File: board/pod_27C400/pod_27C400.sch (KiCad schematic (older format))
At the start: 13 parts, among them J1 EXT_D, J2 EXT_ADDR, J3 VCC_Probe, J4 GND_Probe, J5 ROM Lines, U1 74HCT02

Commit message: Added pod for 27C400, modified other pods
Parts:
- removed J5: ROM Lines, Connector_PinHeader_2.54mm:PinHeader_2x14_P2.54mm_Vertical, symbol Connector_Generic:Conn_02x14_Odd_Even
- added J5: ROM Lines, Connector_PinHeader_2.54mm:PinHeader_2x20_P2.54mm_Vertical, symbol Connector_Generic:Conn_02x20_Odd_Even
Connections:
- wire segments 203 -> 216
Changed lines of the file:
@@
 Wire Wire Line
 	7050 2100 7200 2100
-$Comp
-L Connector_Generic:Conn_02x14_Odd_Even J5
-U 1 1 5FE5E217
-P 6500 3700
-F 0 "J5" H 6550 4517 50  0000 C CNN
-F 1 "ROM Lines" H 6550 4426 50  0000 C CNN
-F 2 "Connector_PinHeader_2.54mm:PinHeader_2x14_P2.54mm_Vertical" H 6500 3700 50  0001 C CNN
-F 3 "~" H 6500 3700 50  0001 C CNN
-	1    6500 3700
-	1    0    0    -1
-$EndComp
-Wire Wire Line
-	6800 3100 7200 3100
-Text Label 7200 3100 2    50   ~ 0
+Wire Wire Line
+	6950 5000 7350 5000
+Text Label 7350 5000 2    50   ~ 0
 EXT_VCC
-Wire Wire Line
-	6800 3200 7200 3200
-Wire Wire Line
-	6800 3300 7200 3300
-Wire Wire Line
-	6800 3400 7200 3400
-Wire Wire Line
-	6800 3500 7200 3500
-Wire Wire Line
-	6800 3600 7200 3600
-Wire Wire Line
-	6800 3700 7200 3700
-Wire Wire Line
-	6800 3800 7200 3800
-Wire Wire Line
-	6800 3900 7200 3900
-Wire Wire Line
-	6800 4000 7200 4000
-Wire Wire Line
-	6800 4100 7200 4100
-Wire Wire Line
-	6800 4200 7200 4200
-Wire Wire Line
-	6800 4300 7200 4300
-Wire Wire Line
-	6800 4400 7200 4400
-Wire Wire Line
-	6300 3100 5800 3100
-Wire Wire Line
-	6300 3200 5800 3200
-Wire Wire Line
-	6300 3300 5800 3300
-Wire Wire Line
-	6300 3400 5800 3400
-Wire Wire Line
-	6300 3500 5800 3500
-Wire Wire Line
-	6300 3600 5800 3600
-Wire Wire Line
-	6300 3700 5800 3700
-Wire Wire Line
-	6300 3800 5800 3800
-Wire Wire Line
-	6300 3900 5800 3900
-Wire Wire Line
-	6300 4000 5800 4000
-Wire Wire Line
-	6300 4100 5800 4100
-Wire Wire Line
-	6300 4200 5800 4200
-Wire Wire Line
-	6300 4300 5800 4300
-Wire Wire Line
-	6300 4400 5800 4400
 $Comp
 L power:GND #PWR0113
 U 1 1 5FFADC5E
-P 5800 4500
-F 0 "#PWR0113" H 5800 4250 50  0001 C CNN
-F 1 "GND" H 5805 4327 50  0000 C CNN
-F 2 "" H 5800 4500 50  0001 C CNN
-F 3 "" H 5800 4500 50  0001 C CNN
-	1    5800 4500
-	1    0    0    -1
-$EndComp
-Wire Wire Line
-	5800 4400 5800 4500
-Text Label 5800 3100 0    50   ~ 0
-A15
-Text Label 5800 3200 0    50   ~ 0
-A12
-Text Label 5800 3300 0    50   ~ 0
-A7
-Text Label 5800 3400 0    50   ~ 0
-A6
-Text Label 5800 3500 0    50   ~ 0
-A5
-Text Label 5800 3600 0    50   ~ 0
-A4
-Text Label 5800 3700 0    50   ~ 0
-A3
-Text Label 5800 3800 0    50   ~ 0
-A2
-Text Label 5800 3900 0    50   ~ 0
-A1
-Text Label 5800 4000 0    50   ~ 0
-A0
-Text Label 5800 4100 0    50   ~ 0
-D0
-Text Label 5800 4200 0    50   ~ 0
-D1
-Text Label 5800 4300 0    50   ~ 0
-D2
-Text Label 7200 4400 2    50   ~ 0
-D3
-Text Label 7200 4300 2    50   ~ 0
-D4
-Text Label 7200 4200 2    50   ~ 0
-D5
-Text Label 7200 4100 2    50   ~ 0
-D6
-Text Label 7200 4000 2    50   ~ 0
-D7
-Text Label 7200 3900 2    50   ~ 0
-~DIR_CE
-Text Label 7200 3800 2    50   ~ 0
-A10
-Text Label 7200 3700 2    50   ~ 0
-~OE
-Text Label 7200 3600 2    50   ~ 0
-A11
-Text Label 7200 3500 2    50   ~ 0
-A9
-Text Label 7200 3400 2    50   ~ 0
-A8
-Text Label 7200 3300 2    50   ~ 0
-A13
-Text Label 7200 3200 2    50   ~ 0
-A14
+P 7550 4200
+F 0 "#PWR0113" H 7550 3950 50  0001 C CNN
+F 1 "GND" H 7555 4027 50  0000 C CNN
+F 2 "" H 7550 4200 50  0001 C CNN
+F 3 "" H 7550 4200 50  0001 C CNN
+	1    7550 4200
+	1    0    0    -1
+$EndComp
 $Comp
 L Device:LED_Small D1
@@
 Wire Wire Line
 	1950 3000 2250 3000
+$Comp
+L Connector_Generic:Conn_02x20_Odd_Even J5
+U 1 1 5FFBAEB6
+P 6650 4000
+F 0 "J5" H 6700 5117 50  0000 C CNN
+F 1 "ROM Lines" H 6700 5026 50  0000 C CNN
+F 2 "Connector_PinHeader_2.54mm:PinHeader_2x20_P2.54mm_Vertical" H 6650 4000 50  0001 C CNN
+F 3 "~" H 6650 4000 50  0001 C CNN
+	1    6650 4000
+	1    0    0    -1
+$EndComp
+Wire Wire Line
+	7550 4100 7550 4200
+$Comp
+L power:GND #PWR?
+U 1 1 60054FB5
+P 5900 4200
+F 0 "#PWR?" H 5900 3950 50  0001 C CNN
+F 1 "GND" H 5905 4027 50  0000 C CNN
+F 2 "" H 5900 4200 50  0001 C CNN
+F 3 "" H 5900 4200 50  0001 C CNN
+	1    5900 4200
+	1    0    0    -1
+$EndComp
+Wire Wire Line
+	5900 4100 5900 4200
+Wire Wire Line
+	6950 4000 7450 4000
+Text Label 7450 4000 2    50   ~ 0
+A18
+Wire Wire Line
+	6950 3100 7450 3100
+Wire Wire Line
+	6950 3200 7450 3200
+Wire Wire Line
+	6950 3300 7450 3300
+Wire Wire Line
+	6950 3400 7450 3400
+Wire Wire Line
+	6950 3500 7450 3500
+Wire Wire Line
+	6950 3600 7450 3600
+Wire Wire Line
+	6950 3700 7450 3700
+Wire Wire Line
+	6950 3800 7450 3800
+Wire Wire Line
+	6950 3900 7450 3900
+Wire Wire Line
+	6950 4100 7550 4100
+Wire Wire Line
+	6950 4200 7450 4200
+Wire Wire Line
+	6950 4300 7450 4300
+Wire Wire Line
+	6950 4400 7450 4400
+Wire Wire Line
+	6950 4500 7450 4500
+Wire Wire Line
+	6950 4600 7450 4600
+Wire Wire Line
+	6950 4700 7450 4700
+Wire Wire Line
+	6950 4800 7450 4800
+Wire Wire Line
+	6950 4900 7450 4900
+Text Label 7450 3100 2    50   ~ 0
+A8
+Text Label 7450 3200 2    50   ~ 0
+A9
+Text Label 7450 3300 2    50   ~ 0
+A10
+Text Label 7450 3400 2    50   ~ 0
+A11
+Text Label 7450 3500 2    50   ~ 0
+A12
+Text Label 7450 3600 2    50   ~ 0
+A13
+Text Label 7450 3700 2    50   ~ 0
+A14
+Text Label 7450 3800 2    50   ~ 0
+A15
+Text Label 7450 3900 2    50   ~ 0
+A16
+Wire Wire Line
+	6450 3100 6000 3100
+Wire Wire Line
+	6450 3200 6000 3200
+Wire Wire Line
+	6450 3300 6000 3300
+Wire Wire Line
+	6450 3400 6000 3400
+Wire Wire Line
+	6450 3500 6000 3500
+Wire Wire Line
+	6450 3600 6000 3600
+Wire Wire Line
+	6450 3700 6000 3700
+Wire Wire Line
+	6450 3800 6000 3800
+Wire Wire Line
+	6450 3900 6000 3900
+Wire Wire Line
+	6450 4000 6000 4000
+Wire Wire Line
+	6450 4200 6000 4200
+Wire Wire Line
+	6450 4300 6000 4300
+Wire Wire Line
+	6450 4400 6000 4400
+Wire Wire Line
+	6450 4500 6000 4500
+Wire Wire Line
+	6450 4600 6000 4600
+Wire Wire Line
+	6450 4700 6000 4700
+Wire Wire Line
+	6450 4800 6000 4800
+Wire Wire Line
+	6450 4900 6000 4900
+Wire Wire Line
+	6450 5000 6000 5000
+Text Label 6000 3100 0    50   ~ 0
+A17
+Text Label 6000 3200 0    50   ~ 0
+A7
+Text Label 6000 3300 0    50   ~ 0
+A6
+Text Label 6000 3400 0    50   ~ 0
+A5
+Text Label 6000 3500 0    50   ~ 0
+A4
+Text Label 6000 3600 0    50   ~ 0
+A3
+Text Label 6000 3700 0    50   ~ 0
+A2
+Text Label 6000 3800 0    50   ~ 0
+A1
+Text Label 6000 3900 0    50   ~ 0
+A0
+Text Label 6000 4000 0    50   ~ 0
+~DIR_CE
+Wire Wire Line
+	5900 4100 6450 4100
+Text Label 6000 4200 0    50   ~ 0
+~OE
+Text Label 6000 4300 0    50   ~ 0
+D0
+Text Label 6000 4400 0    50   ~ 0
+D8
+Text Label 6000 4500 0    50   ~ 0
+D1
+Text Label 6000 4600 0    50   ~ 0
+D9
+Text Label 6000 4700 0    50   ~ 0
+D2
+Text Label 6000 4800 0    50   ~ 0
+D10
+Text Label 6000 4900 0    50   ~ 0
+D3
+Text Label 6000 5000 0    50   ~ 0
+D11
+Text Label 7450 4900 2    50   ~ 0
+D4
+Text Label 7450 4800 2    50   ~ 0
+D12
+Text Label 7450 4700 2    50   ~ 0
+D5
+Text Label 7450 4600 2    50   ~ 0
+D13
+Text Label 7450 4500 2    50   ~ 0
+D6
+Text Label 7450 4400 2    50   ~ 0
+D14
+Text Label 7450 4300 2    50   ~ 0
+D7
+Text Label 7450 4200 2    50   ~ 0
+D15
 $EndSCHEMATC

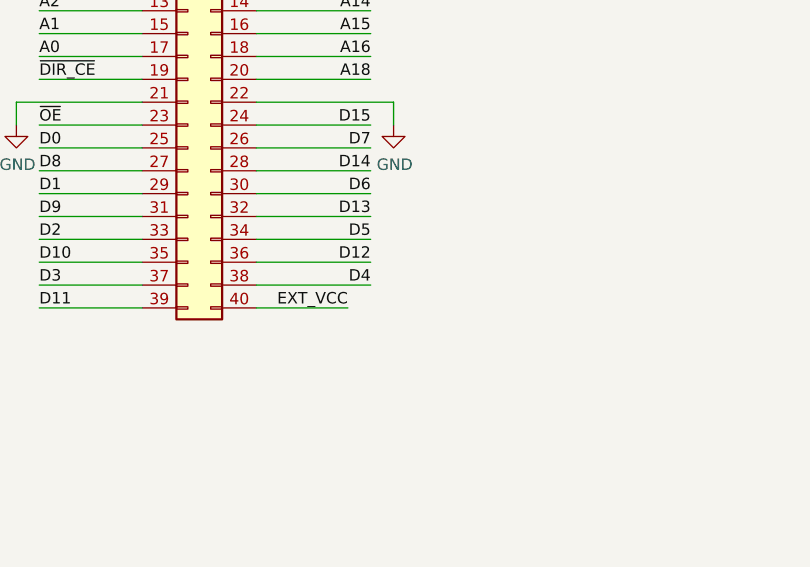
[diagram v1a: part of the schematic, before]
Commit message: Update all the pods to include the diode
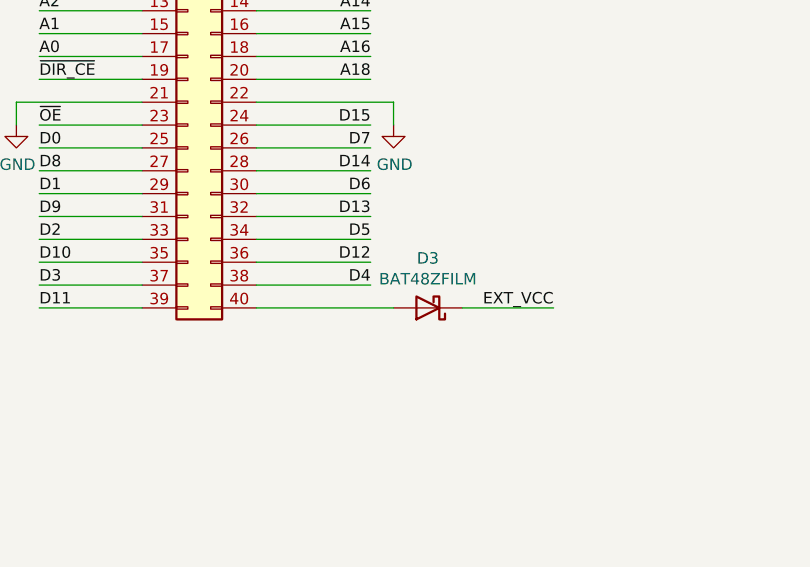
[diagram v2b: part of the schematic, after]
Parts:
- added D3: BAT48ZFILM, Diode_SMD:D_SOD-123, symbol Diode:BAT48ZFILM
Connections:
- net EXT_VCC: now also D3.1 (K); no longer J5.40 (Pin_40)
- new net: D3.2 (A), J5.40 (Pin_40)
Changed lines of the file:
@@
 	7050 2100 7200 2100
 Wire Wire Line
-	6950 5000 7350 5000
-Text Label 7350 5000 2    50   ~ 0
+	7850 5000 8250 5000
+Text Label 8250 5000 2    50   ~ 0
 EXT_VCC
 $Comp
@@
 	7550 4100 7550 4200
 $Comp
-L power:GND #PWR?
+L power:GND #PWR0114
 U 1 1 60054FB5
 P 5900 4200
-F 0 "#PWR?" H 5900 3950 50  0001 C CNN
+F 0 "#PWR0114" H 5900 3950 50  0001 C CNN
 F 1 "GND" H 5905 4027 50  0000 C CNN
 F 2 "" H 5900 4200 50  0001 C CNN
@@
 Text Label 7450 4200 2    50   ~ 0
 D15
+$Comp
+L Diode:BAT48ZFILM D3
+U 1 1 5FE760E2
+P 7700 5000
+F 0 "D3" H 7700 4783 50  0000 C CNN
+F 1 "BAT48ZFILM" H 7700 4874 50  0000 C CNN
+F 2 "Diode_SMD:D_SOD-123" H 7700 4825 50  0001 C CNN
+F 3 "www.st.com/resource/en/datasheet/bat48.pdf" H 7700 5000 50  0001 C CNN
+	1    7700 5000
+	-1   0    0    1
+$EndComp
+Wire Wire Line
+	6950 5000 7550 5000
 $EndSCHEMATC

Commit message: Update 27C400 Pod
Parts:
- removed D1: RED, LED_SMD:LED_1206_3216Metric, symbol Device:LED_Small
- removed R2: 1k, Resistor_SMD:R_1206_3216Metric, symbol Device:R_Small
- added F1: 200mA, Fuse:Fuse_1206_3216Metric, symbol Device:Polyfuse_Small
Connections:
- net VCC: now also R1.2, U1.2, U1.3, F1.1
- removed net EXT_VCC: D3.1 (K), R1.2, U1.2, U1.3
- new net: D3.1 (K), F1.2
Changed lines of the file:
@@
 Title ""
 Date ""
-Rev ""
+Rev "1.1"
 Comp ""
 Comment1 ""
@@
 Wire Wire Line
 	5300 1350 5300 1450
-Text Label 4750 1350 0    50   ~ 0
-EXT_VCC
 $Comp
 L Device:R_Small R1
@@
 Wire Wire Line
 	5150 1650 5150 1350
-Connection ~ 5150 1350
-Wire Wire Line
-	5150 1350 4750 1350
 $Comp
 L power:GND #PWR0109
@@
 Wire Wire Line
 	7050 2100 7200 2100
-Wire Wire Line
-	7850 5000 8250 5000
-Text Label 8250 5000 2    50   ~ 0
-EXT_VCC
 $Comp
 L power:GND #PWR0113
@@
 	1    0    0    -1
 $EndComp
-$Comp
-L Device:LED_Small D1
-U 1 1 601944B8
-P 1550 2550
-F 0 "D1" H 1550 2785 50  0000 C CNN
-F 1 "RED" H 1550 2694 50  0000 C CNN
-F 2 "LED_SMD:LED_1206_3216Metric" V 1550 2550 50  0001 C CNN
-F 3 "~" V 1550 2550 50  0001 C CNN
-	1    1550 2550
-	1    0    0    -1
-$EndComp
-$Comp
-L Device:R_Small R2
-U 1 1 6019F326
-P 1850 2550
-F 0 "R2" V 2046 2550 50  0000 C CNN
-F 1 "1k" V 1955 2550 50  0000 C CNN
-F 2 "Resistor_SMD:R_1206_3216Metric" H 1850 2550 50  0001 C CNN
-F 3 "~" H 1850 2550 50  0001 C CNN
-	1    1850 2550
-	0    -1   -1   0
-$EndComp
-Wire Wire Line
-	1750 2550 1650 2550
-$Comp
-L power:GND #PWR0115
-U 1 1 601B232D
-P 1350 2600
-F 0 "#PWR0115" H 1350 2350 50  0001 C CNN
-F 1 "GND" H 1355 2427 50  0000 C CNN
-F 2 "" H 1350 2600 50  0001 C CNN
-F 3 "" H 1350 2600 50  0001 C CNN
-	1    1350 2600
-	1    0    0    -1
-$EndComp
-Wire Wire Line
-	1450 2550 1350 2550
-Wire Wire Line
-	1350 2550 1350 2600
-Wire Wire Line
-	1950 2550 2400 2550
-Text Label 2400 2550 2    50   ~ 0
-EXT_VCC
 $Comp
 L Device:LED_Small D2
@@
 Wire Wire Line
 	6950 5000 7550 5000
+$Comp
+L power:VCC #PWR0115
+U 1 1 600D4DBB
+P 4750 1200
+F 0 "#PWR0115" H 4750 1050 50  0001 C CNN
+F 1 "VCC" H 4765 1373 50  0000 C CNN
+F 2 "" H 4750 1200 50  0001 C CNN
+F 3 "" H 4750 1200 50  0001 C CNN
+	1    4750 1200
+	1    0    0    -1
+$EndComp
+Wire Wire Line
+	5150 1350 4750 1350
+Wire Wire Line
+	4750 1350 4750 1200
+Connection ~ 5150 1350
+$Comp
+L Device:Polyfuse_Small F1
+U 1 1 600FAA15
+P 8100 4750
+F 0 "F1" H 8168 4796 50  0000 L CNN
+F 1 "200mA" H 8168 4705 50  0000 L CNN
+F 2 "Fuse:Fuse_1206_3216Metric" H 8150 4550 50  0001 L CNN
+F 3 "~" H 8100 4750 50  0001 C CNN
+	1    8100 4750
+	1    0    0    -1
+$EndComp
+Wire Wire Line
+	7850 5000 8100 5000
+Wire Wire Line
+	8100 5000 8100 4850
+$Comp
+L power:VCC #PWR0117
+U 1 1 60129149
+P 8100 4500
+F 0 "#PWR0117" H 8100 4350 50  0001 C CNN
+F 1 "VCC" V 8115 4628 50  0000 L CNN
+F 2 "" H 8100 4500 50  0001 C CNN
+F 3 "" H 8100 4500 50  0001 C CNN
+	1    8100 4500
+	1    0    0    -1
+$EndComp
+Wire Wire Line
+	8100 4650 8100 4500
 $EndSCHEMATC
